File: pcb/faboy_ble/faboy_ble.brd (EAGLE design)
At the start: 85.1 x 54 mm, 56 parts, among them J1 USB-MICROBREDUCED_PASTE, U1 MAX1595UMAX, U2 MCP73831

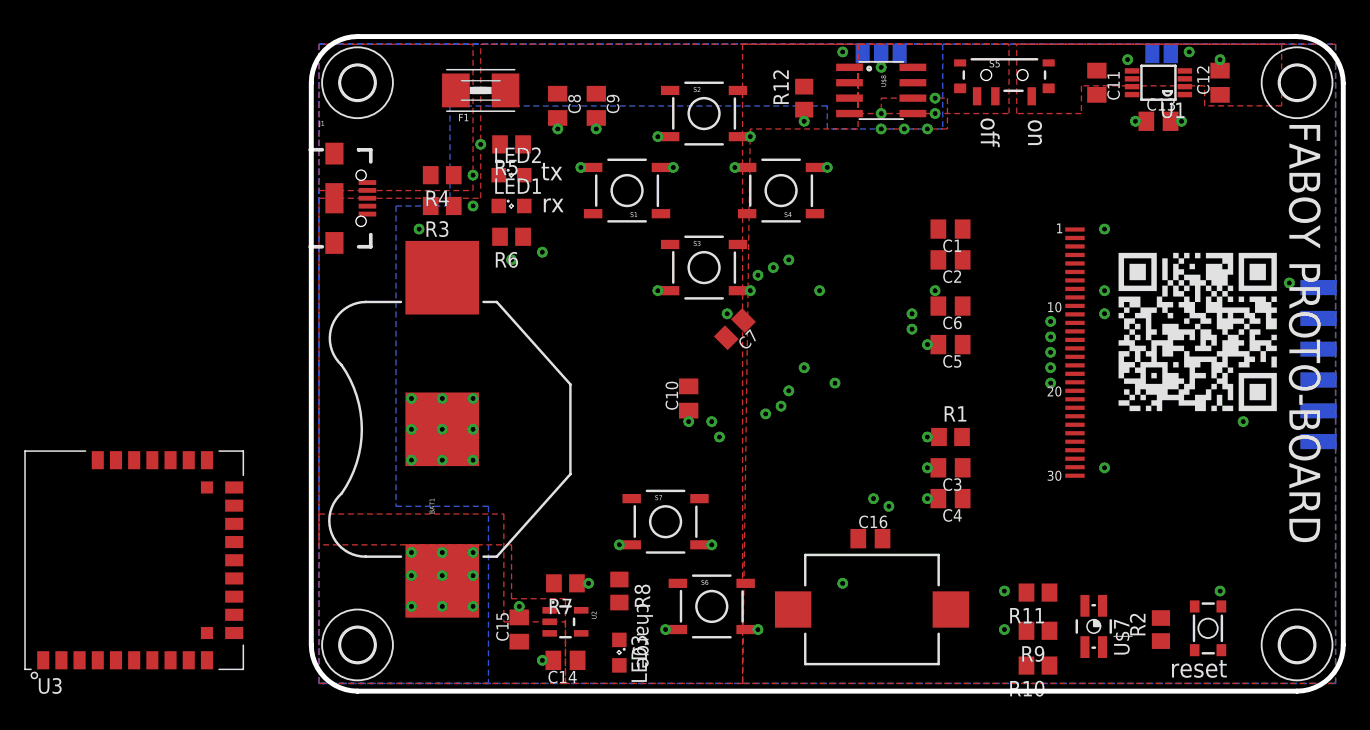
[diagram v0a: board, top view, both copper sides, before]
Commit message: pcb ble routing
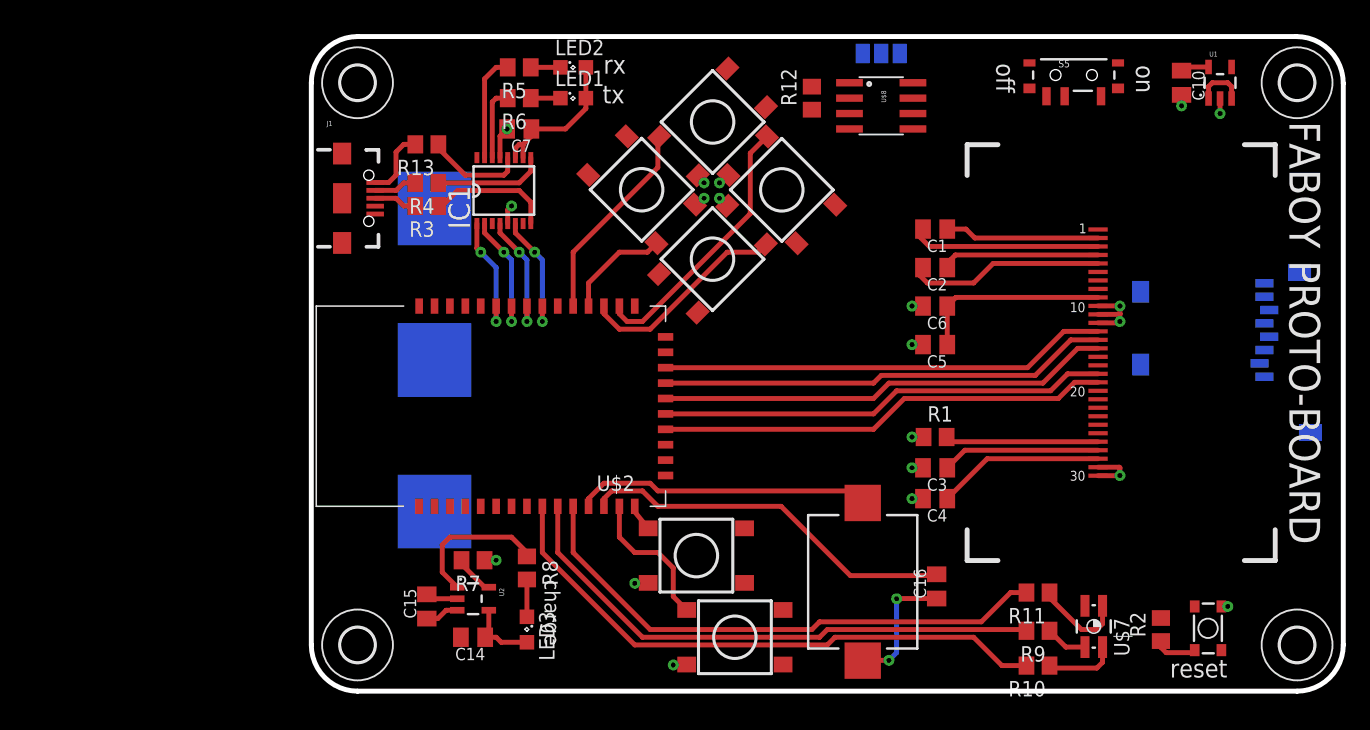
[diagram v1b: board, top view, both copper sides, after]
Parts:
- removed C11: 0.47uF, resistor:C0805K
- removed C12, C13: 2.2uF, resistor:C0805K
- removed C8: 1uF, resistor:C0805K
- removed C9: 0.1uF, resistor:C0805K
- removed F1: 500mA, adafruit:1812
- removed J2: (no value), SparkFun-Connectors:1X06-SMD-FEMALE-V2
- removed SJ1: direct power, jumper:SJ
- removed U3: (no value), BMD-200-Eagle:BMD-200
- added IC1: FT230XS, ftdichip:SSOP16
- added R13: ferrite, resistor:R0805
- added U$2: WT51822-02, Wireless_Tag:WT51822
- added U$9: MICROSD, adafruit:MICROSD
- C10: value 1uF -> 2.2uF
- C7: value 1uF -> 0.1uF
- S1, S2, S3, S4, S6, S7: value SWITCH-MOMENTARY-2SMD-REDUNDANT -> SWITCH-MOMENTARY-2SMD-4; device SparkFun-Electromechanical:TACTILE-SWITCH-SMD -> SparkFun-Electromechanical:TACTILE_SWITCH_TALL
- U1: value MAX1595UMAX -> 3.3V/150mA; device maxim:UMAX8 -> SparkFun-PowerIC:SOT23-5
- moved C10 48.3 mm to (71.8, 50.2), turned to 270 degrees
- moved C7 24.3 mm to (17.1, 46.4), turned to 180 degrees
- moved S1 12.8 mm to (38.8, 41.3), turned to 135 degrees
- moved S3 12.0 mm to (33.1, 46.9), turned to 225 degrees
- moved S2 12.0 mm to (33.1, 35.6), turned to 45 degrees
- moved S4 11.5 mm to (27.2, 41.3), turned to 315 degrees
- moved R6 11.4 mm to (17.1, 48.9)
- moved LED1 10.2 mm to (21.6, 48.9)
- moved LED2 10.2 mm to (21.6, 51.4)
- moved C15 7.85 mm to (9.53, 6.99)
- moved C14 7.85 mm to (13.3, 4.45)
- moved LED3 7.85 mm to (17.8, 5.08)
- moved R7 7.85 mm to (13.3, 10.8)
- moved R8 7.85 mm to (17.8, 10.2)
- moved U2 7.85 mm to (13.3, 7.62)
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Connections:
- removed net N$15: C11.1, U1.6
- removed net N$16: C11.2, U1.7
- removed net N$20: C16.2
- removed net N$26: SG1.2
- new net 3V3: C7.1, IC1.10, IC1.11, IC1.3, LED1.A, LED2.A
- new net CTS: IC1.6, U$2.17
- new net N$11: C16.1, SG1.2
- new net RTS: IC1.2, U$2.19
- new net RX: IC1.4, U$2.18
- new net TX: IC1.1, U$2.20
- net A: now also S7.A2, U$2.40; no longer S7.1, S7.2
- net B: now also S6.A2, U$2.39; no longer S6.1, S6.2
- net BLUE: now also U$2.35
- net CS: now also U$2.8
- net D+: now also IC1.8
- net D-: now also IC1.9
- net DC: now also U$2.6
- net DOWN: now also S4.A2, U$2.14; no longer S1.1, S1.2
- net GND: now also C10.2, C7.2, IC1.13, IC1.5, S1.B2, S2.B2, S3.B2, S4.B2, S6.B2, S7.B2, U$2.11, U$2.27, U$2.29, U$2.30, U$2.31, U1.2; no longer C10.1, C12.2, C13.2, C7.1, C8.2, C9.2, J2.1, S1.3, S1.4, S2.3, S2.4, S3.3, S3.4, S4.3, S4.4, S6.3, S6.4, S7.3, S7.4, U1.4, U1.5
- net GREEN: now also U$2.34
- net LED_RX: now also IC1.15, R5.2; no longer R6.2
- net LED_TX: now also IC1.14, R6.2; no longer R5.2
- net LEFT: now also S3.A2, U$2.15; no longer S2.1, S2.2
- net MISO: now also U$2.3; no longer J2.3
- net MOSI: now also U$2.4; no longer J2.4
- net N$10: now also C16.2, U$2.38; no longer C12.1, S5.3, SJ1.1, U1.2, U1.3
- net N$21: now also U$2.37; no longer C16.1
- net N$9: now also S5.1, U1.1, U1.3; no longer C7.2
- net OLED_RST: now also U$2.7
- net RED: now also U$2.36
- net RIGHT: now also S2.A2, U$2.13; no longer S3.1, S3.2
- net RST: no longer J2.2
- net SCLK: now also U$2.5; no longer J2.5
- net UP: now also S1.A2, U$2.12; no longer S4.1, S4.2
- net VBAT: now also U$2.26
- net VBUS: now also R13.2; no longer F1.1
- net VCC: now also C10.1, U$2.1, U1.5; no longer C13.1, J2.6, LED1.A, LED2.A, SJ1.2, U1.1, U1.8
- net VIN: now also IC1.12, R13.1; no longer C10.2, C8.1, C9.1, F1.2
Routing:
- net GREEN: track 0.00 -> 48.1 mm, vias 2 -> 0
- net BLUE: track 0.00 -> 45.7 mm, vias 2 -> 0
- net RED: track 0.00 -> 45.1 mm, vias 2 -> 0
- net DC: track 0.00 -> 37.4 mm, vias 2 -> 0
- net MOSI: track 0.00 -> 37.3 mm, vias 2 -> 0
- net OLED_RST: track 0.00 -> 37.1 mm, vias 2 -> 0
- net SCLK: track 0.00 -> 37.0 mm, vias 2 -> 0
- net CS: track 0.00 -> 36.9 mm, vias 2 -> 0
- net N$10: track 0.00 -> 31.3 mm, vias 1 -> 0
- net GND: track 0.00 -> 31.2 mm, vias 43 -> 6
- net N$21: track 0.00 -> 24.4 mm
- net UP: track 0.00 -> 22.3 mm
- net VCC: track 0.00 -> 18.3 mm, vias 4 -> 0
- net RIGHT: track 0.00 -> 17.4 mm
- net LEFT: track 0.00 -> 16.9 mm
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- removed copper zone on layer 16, net GND
- removed copper zone on layer 1, net N$10
- removed copper zone on layer 1, net N$28
- removed copper zone on layer 1, net VBAT
- removed copper zone on layer 16, net VBAT
- removed copper zone on layer 1, net VBUS
- removed copper zone on layer 1, net VCC
- removed copper zone on layer 1, net VIN
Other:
- board text removed: "Mayencourt Louis"
- board text removed: "embedded systems engineer"
- board text removed: "louis.mayencourt@gmail.com"

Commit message: ble pcb design done
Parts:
- added C8: 22nF, resistor:C0805K
- added J2: CORTEX_DEBUGSMD, SparkFun-Connectors:SAMTECH_FTSH-105-01
- added R14: 2.2M, resistor:R0805
- added SJ1: conf_2, jumper:SJ
- added TP1, TP2, TP3, TP4, TP5: TPB1,27, testpad:B1,27
- R2: value 10k -> 10M
- SJ3: value direct path -> conf_1
- moved R2 59.1 mm to (11.4, 12.7), turned to 0 degrees
- moved C10 3.81 mm to (75.6, 50.2), turned to 90 degrees
- moved R8 3.42 mm to (19.1, 6.99)
- moved C14 2.84 mm to (14.6, 1.91)
- moved C15 2.84 mm to (10.8, 4.45)
- moved LED3 2.84 mm to (19.1, 2.54)
- moved U2 2.84 mm to (14.6, 5.08)
- moved R7 2.84 mm to (14.6, 8.26)
- moved U1 2.54 mm to (72.4, 50.2), turned to 180 degrees
- moved R12 0.63 mm to (40.6, 48.9)
- moved SJ3 0.25 mm to (47.0, 52.8), turned to 180 degrees
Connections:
- net CS renamed CS_OLED
- new net CS_SD: U$2.3, U$9.2
- new net MES_BAT: C8.1, R14.1, R2.2, TP1.TP, U$2.26
- new net SD_DETECT: U$2.10, U$9.CD1
- new net SWDCLK: J2.4, U$2.21
- new net SWDIO: J2.2, U$2.22
- new net VSS: U$9.6, U$9.MT1, U$9.MT2
- net 3V3: now also SJ3.1
- net GND: now also C8.2, J2.10, J2.3, J2.5, J2.9, R14.2, TP5.TP, U$2.28
- net MISO: now also U$2.9, U$9.7; no longer U$2.3
- net MOSI: now also U$9.3
- net N$9: now also SJ1.1
- net RST: now also U$2.32; no longer R2.1
- net SCLK: now also U$9.5
- net VBAT: now also BAT1.3, R2.1, SJ3.3, TP3.TP; no longer BAT1.1, SJ3.1, U$2.26
- net VCC: now also J2.1, SJ1.2, TP4.TP, U$9.4; no longer R2.2
- net VIN: now also TP2.TP; no longer SJ3.3
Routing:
- net VIN: track 14.2 -> 123.7 mm, vias 0 -> 5
- net VBAT: track 2.79 -> 89.9 mm, vias 0 -> 3
- net RST: track 3.57 -> 65.4 mm, vias 0 -> 2
- net MISO: track 0.00 -> 52.3 mm, vias 0 -> 1
- net CS_SD: track 0.00 -> 51.8 mm, vias 0 -> 1
- net GND: track 31.2 -> 74.3 mm, vias 6 -> 30
- net SD_DETECT: track 0.00 -> 40.8 mm, vias 0 -> 1
- net 3V3: track 12.8 -> 43.0 mm, vias 0 -> 1
- net N$28: track 0.00 -> 27.1 mm, vias 0 -> 1
- net VCC: track 18.3 -> 41.5 mm, vias 0 -> 3
- net SCLK: track 37.0 -> 53.1 mm, vias 0 -> 1
- net VSS: track 0.00 -> 15.9 mm
- net MOSI: track 37.3 -> 52.7 mm, vias 0 -> 1
- net SWDIO: track 0.00 -> 14.4 mm, vias 0 -> 1
- net N$9: track 4.13 -> 18.1 mm, vias 0 -> 1
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- added copper zone on layer 16, net GND
- added copper zone on layer 1, net VBAT
- added copper zone on layer 1, net VCC
- added copper zone on layer 1, net VIN
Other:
- board text added: "0"
- board text added: "1"
- board text added: "2"
- board text added: "A"
- board text added: "AB"
- board text added: "B"
- board text added: "FABOY BLUETOOTH"
- board text added: "GND"
- board text added: "Vbatt"
- board text added: "Vusb"
- board text added: "batt/USB"
- board text added: "battery"
- board text added: "conf"
- board text added: "conf 1"
- board text added: "conf 2"
- board text added: "pile"
- board text added: "pile/USB"
- board text added: "prog"
- board text added: "start"
- board text removed: "FABOY PROTO-BOARD"
- board text removed: "direct path"
- board text removed: "direct power"
- board text removed: "gnd"
- board text removed: "miso"
- board text removed: "mosi"
- board text removed: "reset"
- board text removed: "rst"
- board text removed: "sckl"
- board text removed: "vcc"
